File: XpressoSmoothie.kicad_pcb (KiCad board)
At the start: 2 copper layers, 99.7 x 99.7 mm, 130 parts, among them J1 HEADER_4, J10 HEADER_3X2, J11 Pwr_in, J12 HEADER_4, J13 HEADER_4X2, J14 HEADER_3X2, J15 HEADER_4, J16 HEADER_4, J17 HEADER_4, J172 HEADER_2, J18 HEADER_4, J19 HEADER_2, J2 HEADER_4, J20 HEADER_2, J21 HEADER_2, J22 HEADER_2, J23 HEADER_4, J232 HEADER_2, J24 HEADER_4, J25 HEADER_4, J252 HEADER_2, J26 USB, J27 HEADER_4, J28 MICROSD-MOLEX, J3 HEADER_3, J4 HEADER_3X2, J5 HEADER_3X2, J6 LPCXPRESSO_GENERIC_HEADER, J7 HEADER_4, J8 HEADER_4, J9 HEADER_3X2, M1 LOGO_OSHW, M2 LOGO_OSHW, Q1 IRLB 8743, Q2 IRLB 8743, Q3 IRLB 8743, Q4 IRLB 8743, SW1 SW_PUSH, SW2 SW_PUSH, U1 POLOLU_A4988, U10 TC4422A, U11 TC4422A, U12 LM1117-3.3, U2 POLOLU_A4988, U3 POLOLU_A4988, U4 POLOLU_A4988, U5 POLOLU_A4988, U7 LM7809CT, U8 TC4422A, U9 TC4422A

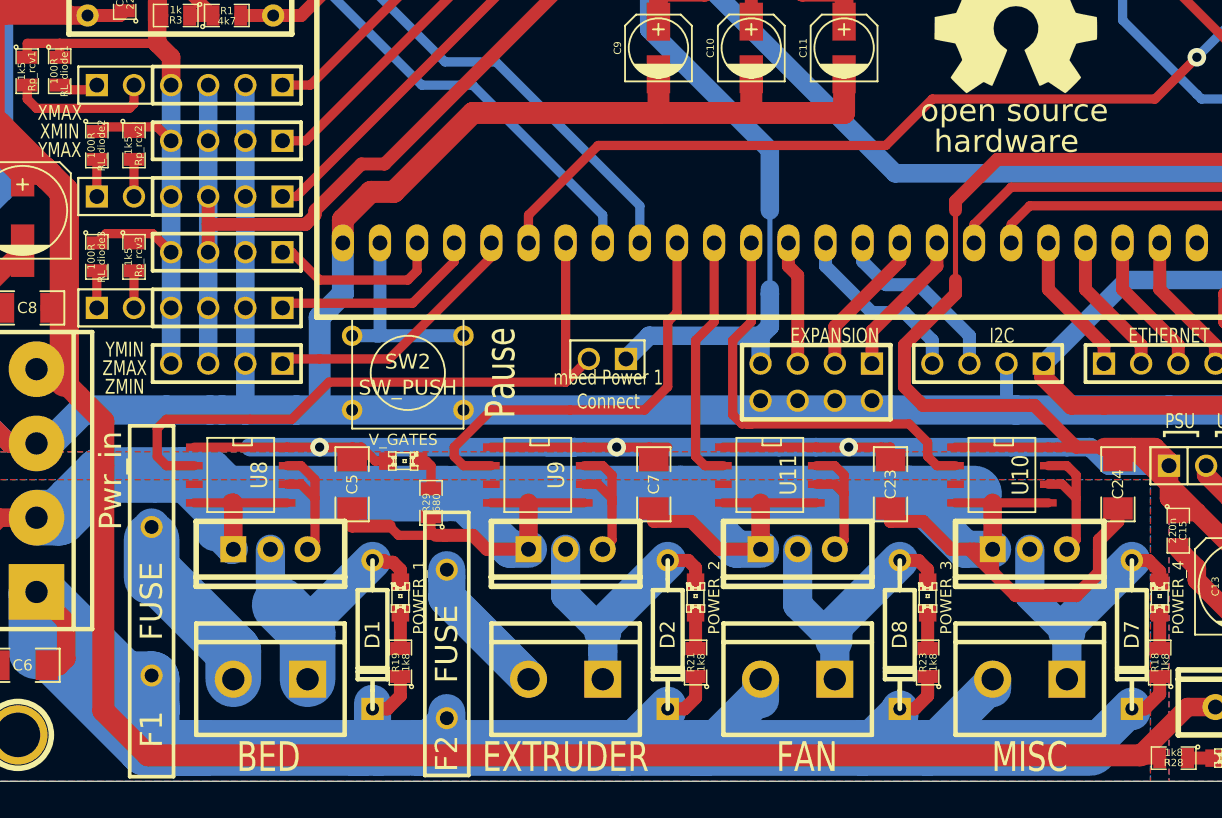
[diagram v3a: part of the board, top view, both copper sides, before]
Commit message: Change 11A fuse footprint to MF-R500 (5A footprint) since that's what fits. Closes #21
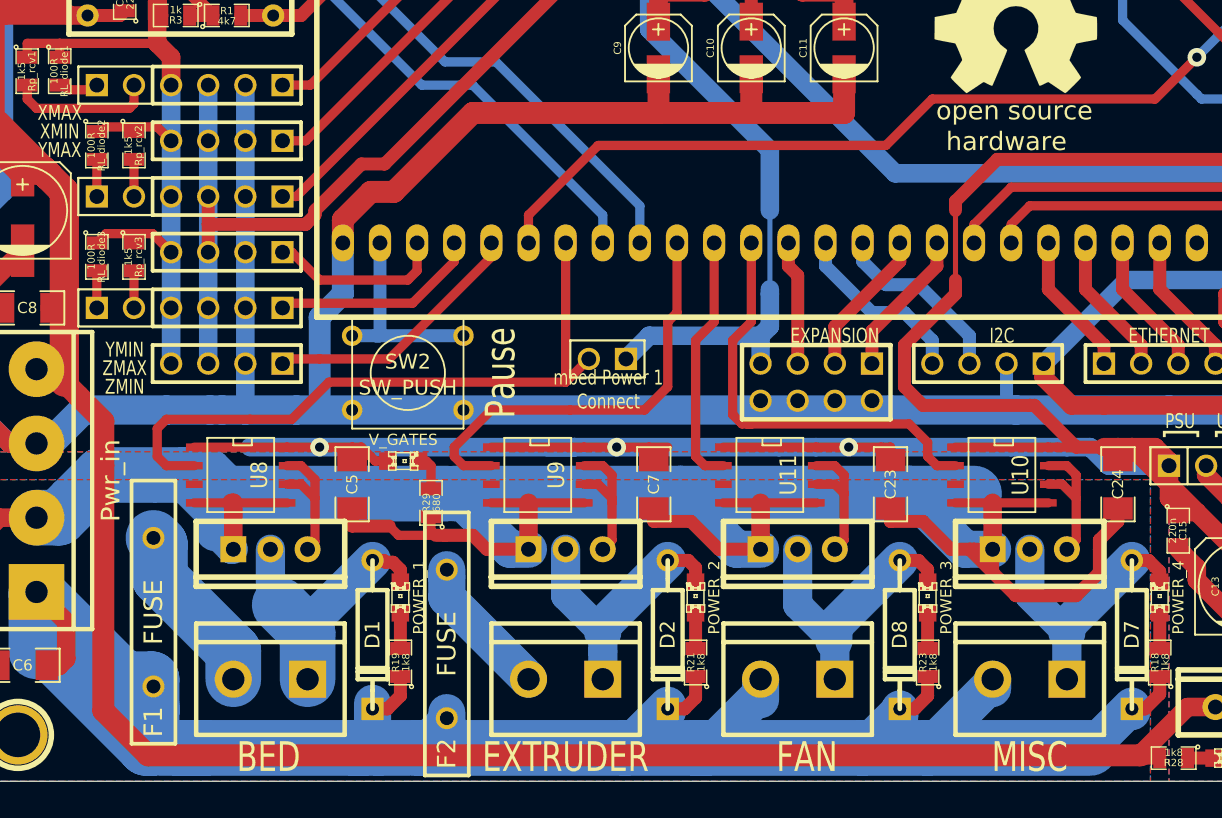
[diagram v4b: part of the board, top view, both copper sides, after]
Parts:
- F1: footprint MF-R1100 -> MF-R500
- moved F1 0.76 mm to (84.2, 142.1)
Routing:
- net N-0000052: track 15.7 -> 12.0 mm

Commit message: Begin routing.
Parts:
- added J29: HEADER_2, PIN_ARRAY_2X1, F.Cu at (104.1, 83.7)
- added JP6: JUMPER-2, PIN_ARRAY_2X1, F.Cu at (109.7, 97.5)
- added JP7: JUMPER-2, PIN_ARRAY_2X1, F.Cu at (121.4, 98.0)
- added JP8: JUMPER-2, PIN_ARRAY_2X1, F.Cu at (111.0, 102.7)
- added JP9: JUMPER-2, PIN_ARRAY_2X1, F.Cu at (111.1, 105.6)
- added SW3: SW_PUSH, SW_PUSH_SMALL, F.Cu at (113.5, 125.7)
- J6: footprint LPCXPRESS0_GENERIC -> LPCXPRESS0_1ROW
- moved JP2 48.4 mm to (100.9, 97.2), turned to 180 degrees
- moved JP1 13.1 mm to (121.2, 113.1)
- moved Th2 10.5 mm to (133.1, 82.8)
- moved D12 10.2 mm to (127.0, 80.0)
- moved R30 9.72 mm to (122.4, 80.0)
- moved Th1 9.28 mm to (138.2, 82.8)
- moved R10 9.14 mm to (121.5, 83.5)
- moved R11 9.14 mm to (118.7, 83.5)
- moved R12 9.14 mm to (115.8, 83.5)
- moved Th0 8.01 mm to (143.3, 82.8)
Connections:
- C9 pad 1: THERM2 -> N-0000091
- J6 pad 10: A-STEP -> N-0000071
- J6 pad 11: A-EN -> A-DIR
- J6 pad 12: Z-DIR -> A-STEP
- J6 pad 13: Z-STEP -> A-EN
- J6 pad 14: Z-EN -> Z-DIR
- J6 pad 19: Y-DIR -> Z-STEP
- J6 pad 20: Y-STEP -> Z-EN
- J6 pad 21: X-EN -> N-0000073
- J6 pad 22: YMAX -> N-0000072
- J6 pad 23: XMIN -> Y-DIR
- J6 pad 24: XMAX -> Y-STEP
- J6 pad 25: B-DIR -> Y-EN
- J6 pad 26: B-STEP -> X-EN
- J6 pad 27: B-EN -> B-DIR
- J6 pad 51: ZMAX -> Bootloader
- J6 pad 52: YMIN -> ZMAX
- J6 pad 9: A-DIR -> N-0000064
- JP1 pad 1: 18_P0.26AOUT -> POWER4
- JP2 pad 1: X-EN -> Y-EN
- JP2 pad 2: A-EN -> X-EN
- R10 pad 1: THERM2 -> N-0000091
- R5 pad 2: X-EN -> Y-EN
- Th2 pad 1: THERM2 -> N-0000091
- U3 pad 9: X-EN -> Y-EN
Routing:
- net +5V: track 141.7 -> 52.3 mm, vias 2 -> 1
- net X-EN: track 108.7 -> 32.5 mm
- net THERM2: track 33.9 -> 0.00 mm
- net YMAX: track 27.2 -> 6.15 mm
- net Y-EN: track 0.00 -> 19.6 mm
- net Y-DIR: track 18.8 -> 0.00 mm
- net Y-STEP: track 18.8 -> 0.00 mm
- net XMIN: track 22.7 -> 5.44 mm
- net Bootloader: track 0.00 -> 16.0 mm
- net GND: track 762.1 -> 747.3 mm
- net XMAX: track 18.0 -> 4.92 mm
- net Z-STEP: track 21.8 -> 33.6 mm
- net N-0000091: track 0.00 -> 11.0 mm
- net 18_P0.26AOUT: track 45.5 -> 35.6 mm
- net Z-EN: track 36.5 -> 27.4 mm
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
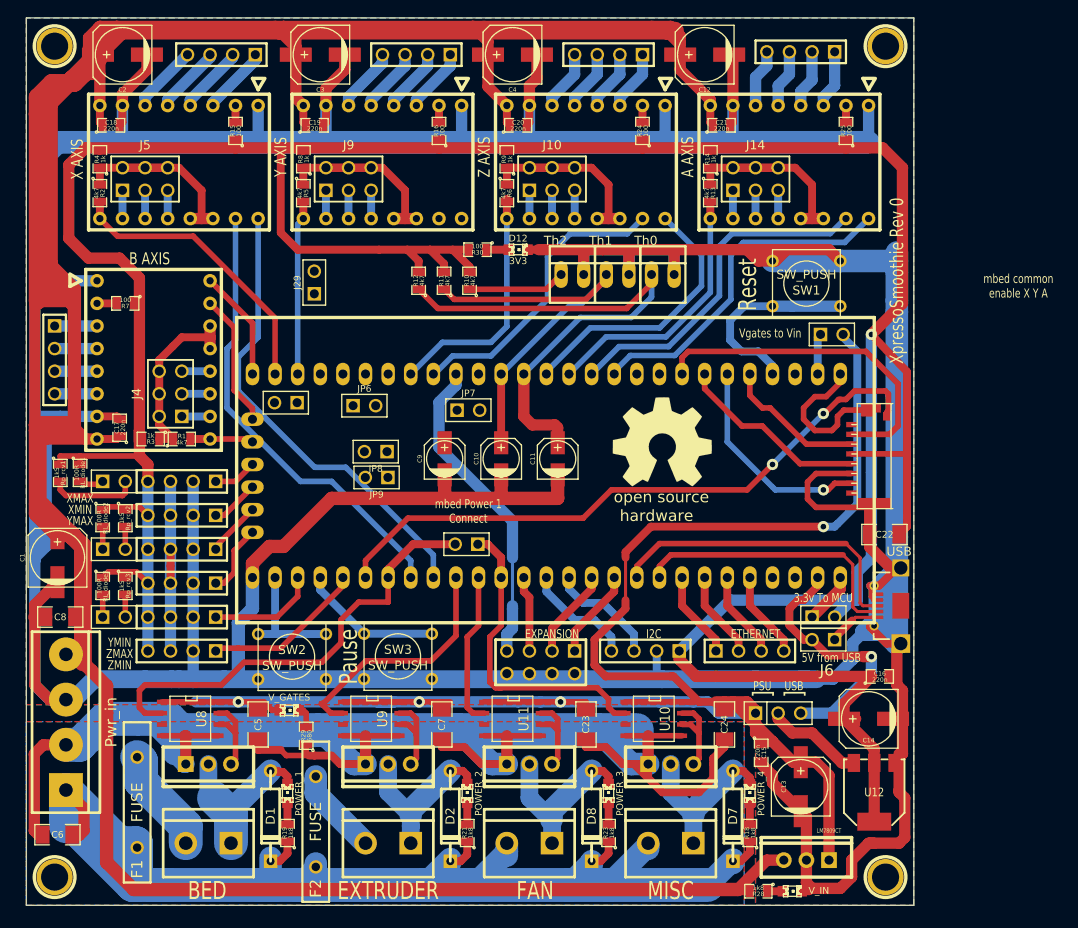
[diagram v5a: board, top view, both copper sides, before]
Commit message: Finished routing new pin assignments and jumpers and stuff.
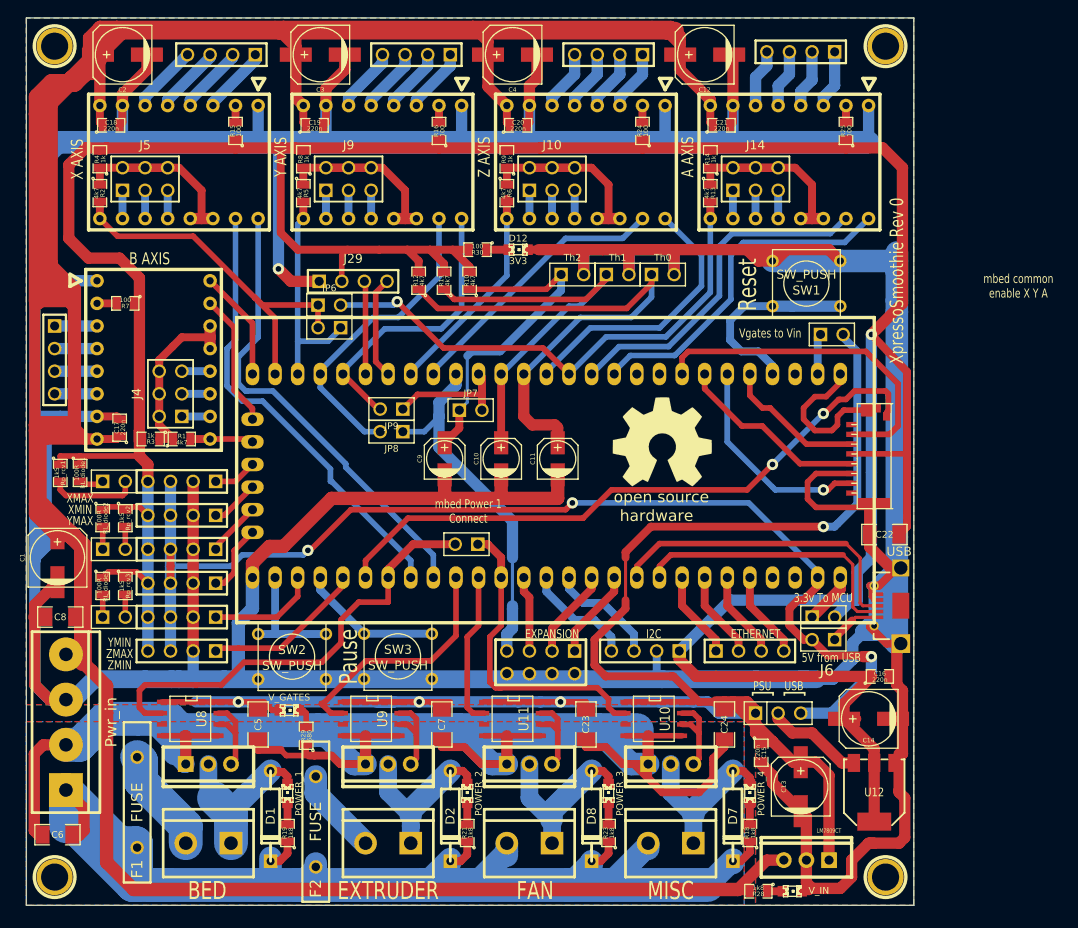
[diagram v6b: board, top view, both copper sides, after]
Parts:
- J29: value HEADER_2 -> HEADER_4; footprint PIN_ARRAY_2X1 -> PIN_ARRAY_4x1
- Th0, Th1, Th2: footprint PINHEAD1-2 -> PIN_ARRAY_2X1
- moved JP6 12.0 mm to (105.8, 86.2)
- moved JP2 9.74 mm to (105.8, 88.8)
- moved JP9 7.86 mm to (112.8, 97.9)
- moved J29 4.36 mm to (108.5, 83.6), turned to 0 degrees
- moved JP8 2.86 mm to (112.8, 100.5)
- moved JP7 0.25 mm to (121.7, 98.0)
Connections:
- J29 pad 1: N-0000072 -> GND
- J29 pad 2: N-0000073 -> +3.3VP
- J6 pad 21: N-0000073 -> N-0000092
- J6 pad 22: N-0000072 -> N-0000093
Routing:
- net +5V: track 52.3 -> 131.8 mm, vias 1 -> 3
- net Y-STEP: track 0.00 -> 34.9 mm
- net Y-DIR: track 0.00 -> 32.5 mm
- net A-EN: track 29.9 -> 59.0 mm, vias 0 -> 1
- net N-0000094: track 11.0 -> 37.1 mm
- net GND: track 747.3 -> 767.1 mm, vias 0 -> 1
- net THERM2: track 0.00 -> 13.8 mm
- net +3.3VP: track 383.3 -> 394.9 mm
- net N-0000092: track 0.00 -> 11.5 mm
- net N-0000093: track 0.00 -> 10.5 mm
- net X-EN: track 32.5 -> 42.6 mm
- net Y-EN: track 19.6 -> 25.2 mm
- net 18_P0.26AOUT: track 35.6 -> 40.3 mm
- net Z-EN: track 27.4 -> 24.2 mm
- net Z-STEP: track 33.6 -> 31.0 mm
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
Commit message: Added notes on silkscreen for jumpers. After one or two additional checks, I'll officially call it revision 1.
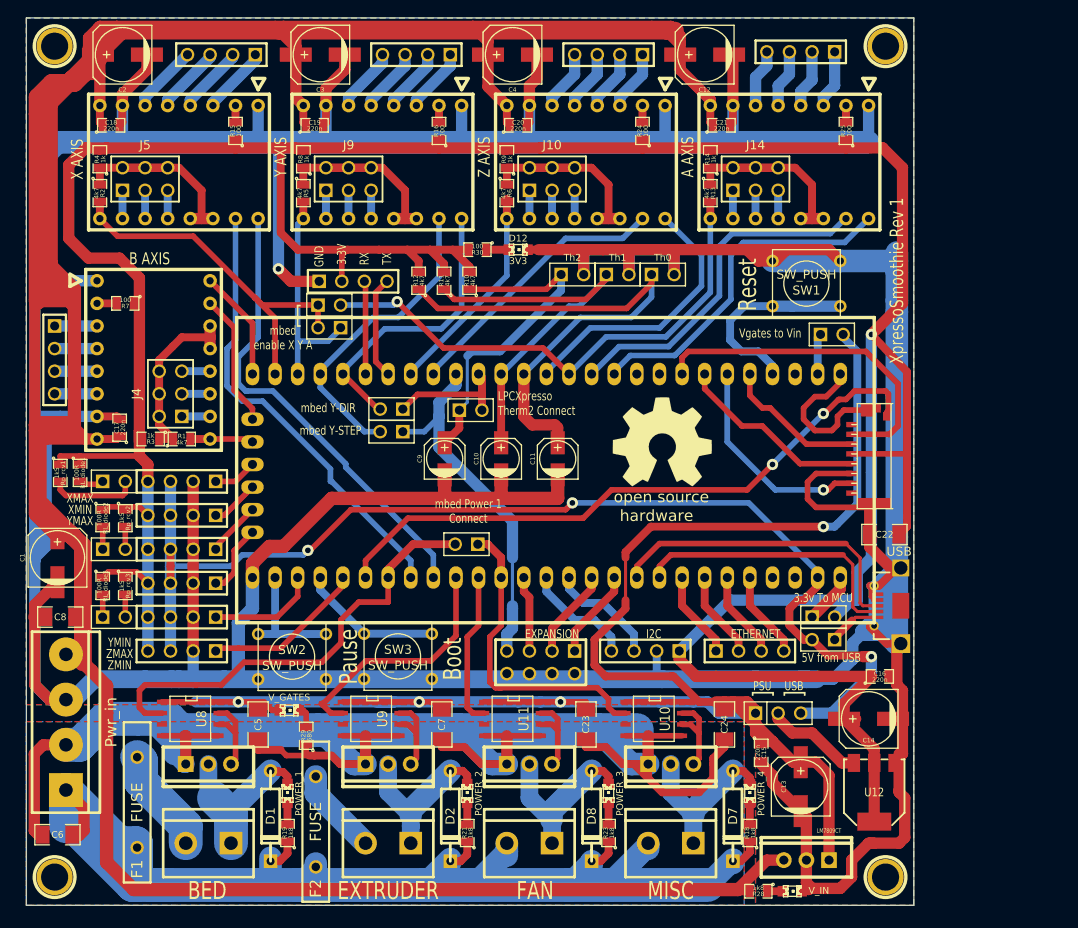
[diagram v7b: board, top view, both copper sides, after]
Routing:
- net +3.3VP: track 394.9 -> 395.5 mm
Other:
- board text added: "3.3V"
- board text added: "Boot"
- board text added: "GND"
- board text added: "LPCXpresso Therm2 Connect"
- board text added: "RX"
- board text added: "TX"
- board text added: "XpressoSmoothie Rev 1"
- board text added: "mbed Y-DIR"
- board text added: "mbed Y-STEP"
- board text added: "mbed enable X Y A"
- board text removed: "XpressoSmoothie Rev 0"
- board text removed: "mbed common enable X Y A"
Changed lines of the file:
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@@
   (general
     (links 359)
-    (no_connects 6)
-    (area 71.742299 53.962299 171.462701 153.682701)
+    (no_connects 5)
+    (area 56.388 52.51262 187.467201 163.2712)
     (thickness 1.6)
-    (drawings 36)
-    (tracks 1305)
+    (drawings 45)
+    (tracks 1306)
     (zones 0)
     (modules 136)
@@
   (module LPCXPRESS0_1ROW   locked (layer F.Cu)
     (at 167.005 87.63 180)
-    (fp_text reference J6 (at 5.334 -39.624 180) (layer F.SilkS)
+    (fp_text reference J6 (at 5.334 -39.624 180) (layer F.SilkS) hide
       (effects (font (thickness 0.3048)))
     )
@@
     (descr "Connecteurs 2 pins")
     (tags "CONN DEV")
-    (fp_text reference JP6 (at 0 -1.905) (layer F.SilkS)
+    (fp_text reference JP6 (at 0 -1.905) (layer F.SilkS) hide
       (effects (font (size 0.762 0.762) (thickness 0.1524)))
     )
@@
     (descr "Connecteurs 2 pins")
     (tags "CONN DEV")
-    (fp_text reference JP7 (at 0 -1.905) (layer F.SilkS)
+    (fp_text reference JP7 (at 0 -1.905) (layer F.SilkS) hide
       (effects (font (size 0.762 0.762) (thickness 0.1524)))
     )
@@
     (descr "Connecteurs 2 pins")
     (tags "CONN DEV")
-    (fp_text reference JP8 (at 0 -1.905 180) (layer F.SilkS)
+    (fp_text reference JP8 (at 0 -1.905 180) (layer F.SilkS) hide
       (effects (font (size 0.762 0.762) (thickness 0.1524)))
     )
@@
     (descr "Connecteurs 2 pins")
     (tags "CONN DEV")
-    (fp_text reference JP9 (at 0 -1.905 180) (layer F.SilkS)
+    (fp_text reference JP9 (at 0 -1.905 180) (layer F.SilkS) hide
       (effects (font (size 0.762 0.762) (thickness 0.1524)))
     )
@@
     (descr "Double rangee de contacts 2 x 5 pins")
     (tags CONN)
-    (fp_text reference J29 (at 0 -2.54) (layer F.SilkS)
+    (fp_text reference J29 (at 0 -2.54) (layer F.SilkS) hide
       (effects (font (size 1.016 1.016) (thickness 0.2032)))
     )
@@
     )
   )
+  (gr_text "mbed Y-STEP" (at 105.918 100.33) (layer F.SilkS)
+    (effects (font (size 1.016 0.762) (thickness 0.1524)))
+  )
+  (gr_text "mbed Y-DIR" (at 105.664 97.79) (layer F.SilkS)
+    (effects (font (size 1.016 0.762) (thickness 0.1524)))
+  )
+  (gr_text "LPCXpresso\nTherm2 Connect" (at 124.714 97.282) (layer F.SilkS)
+    (effects (font (size 1.016 0.762) (thickness 0.1524)) (justify left))
+  )
+  (gr_text TX (at 112.268 81.026 90) (layer F.SilkS)
+    (effects (font (size 1.016 0.762) (thickness 0.1524)))
+  )
+  (gr_text RX (at 109.728 81.026 90) (layer F.SilkS)
+    (effects (font (size 1.016 0.762) (thickness 0.1524)))
+  )
+  (gr_text 3.3V (at 107.188 80.518 90) (layer F.SilkS)
+    (effects (font (size 1.016 0.762) (thickness 0.1524)))
+  )
+  (gr_text GND (at 104.648 80.772 90) (layer F.SilkS)
+    (effects (font (size 1.016 0.762) (thickness 0.1524)))
+  )
+  (gr_text [ (at 102.362 87.376) (layer F.SilkS)
+    (effects (font (size 2.032 1.524) (thickness 0.3048)))
+  )
+  (gr_text Boot (at 119.634 125.984 90) (layer F.SilkS)
+    (effects (font (size 2.032 1.524) (thickness 0.3048)))
+  )
   (gr_text "mbed Power 1\nConnect" (at 121.4 109.4) (layer F.SilkS)
     (effects (font (size 1.016 0.762) (thickness 0.1524)))
@@
     (effects (font (size 1.016 0.762) (thickness 0.1524)))
   )
-  (gr_text "mbed common\nenable X Y A" (at 183.2 84.1) (layer F.SilkS)
+  (gr_text "mbed\nenable X Y A" (at 100.584 89.916) (layer F.SilkS)
     (effects (font (size 1.016 0.762) (thickness 0.1524)))
   )
@@
     (effects (font (size 2.032 1.524) (thickness 0.3048)))
   )
-  (gr_text "XpressoSmoothie Rev 0" (at 169.545 83.5025 90) (layer F.SilkS)
+  (gr_text "XpressoSmoothie Rev 1" (at 169.545 83.5025 90) (layer F.SilkS)
     (effects (font (size 1.524 1.143) (thickness 0.2286)))
   )
@@
     (arrow2b (pts (xy 64.770001 53.975) (xy 65.356421 55.101503)))
   )
+  (segment (start 121.4755 80.01) (end 120.904 80.01) (width 0.635) (layer F.Cu) (net 1))
+  (segment (start 120.904 80.01) (end 119.634 80.01) (width 0.889) (layer F.Cu) (net 1))
   (segment (start 148.59 68.8975) (end 148.2725 68.8975) (width 0.889) (layer F.Cu) (net 1))
   (segment (start 129.54 68.58) (end 126.0475 68.58) (width 0.635) (layer F.Cu) (net 1))
@@
   (segment (start 121.539 82.55) (end 121.539 81.915) (width 0.889) (layer F.Cu) (net 1))
   (segment (start 121.539 81.915) (end 119.634 80.01) (width 0.889) (layer F.Cu) (net 1))
-  (segment (start 120.904 80.01) (end 119.634 80.01) (width 0.889) (layer F.Cu) (net 1))
   (segment (start 119.634 80.01) (end 117.094 80.01) (width 0.889) (layer F.Cu) (net 1))
   (segment (start 163.83 68.58) (end 140.97 68.58) (width 1.27) (layer F.Cu) (net 1))
